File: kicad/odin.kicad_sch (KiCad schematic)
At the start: 0 parts

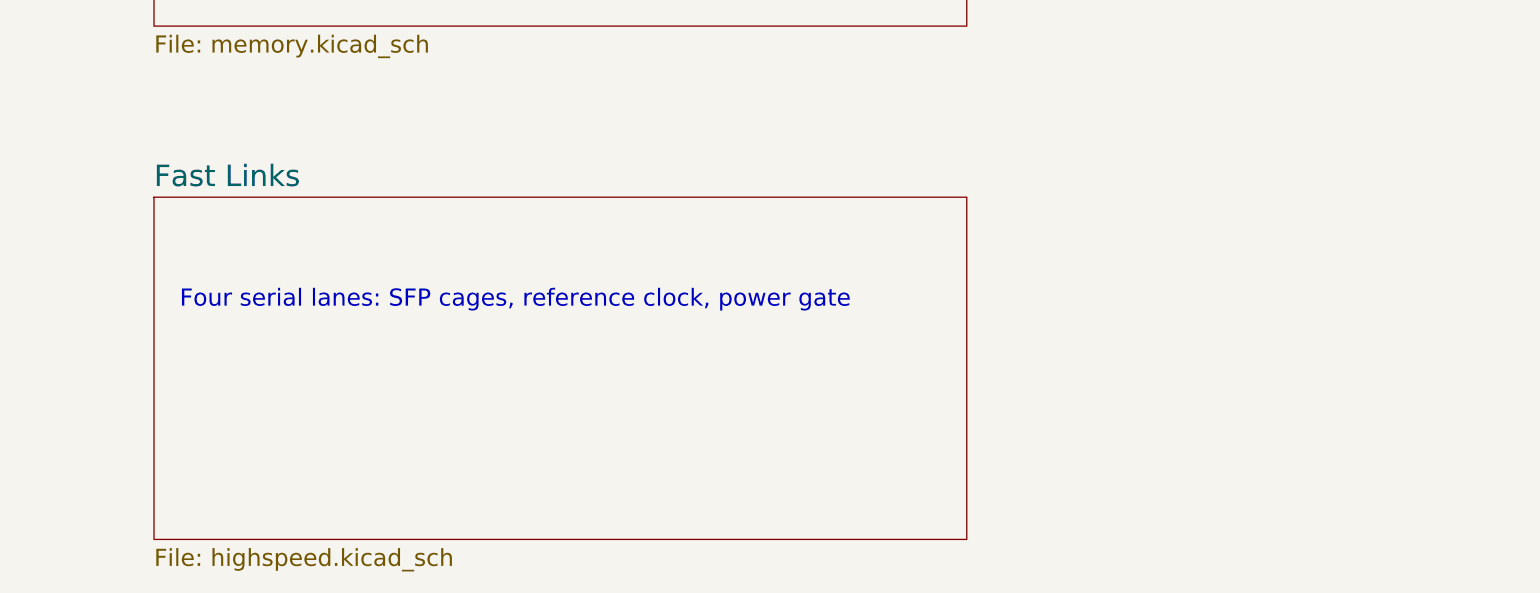
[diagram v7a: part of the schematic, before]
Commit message: Fast Links out, Network in: RTL8211FD-CG on RGMII, ETH jack, LINK P and LINK Q
The two SFP ports, their cages, the 125 MHz oscillator, the power gate and
the I2C switch leave the design, and with them the SFP nets on the board
controller (GPIO32-39 and 46 are spare, GPIO14/31 carry the status expander's
I2C). Both GTP quads stay powered per UG482 with grounded RX and one RCAL
each.

A Network sheet replaces them: an RTL8211FD-CG gigabit PHY on RGMII at 2.5 V
with its straps, reset, interrupt, MDIO pull-up, crystal and jack LEDs wired
from the datasheet rev 1.7 tables, a HanRun HR911130A 1000Base-T magjack,
and two plain shielded 8P8C jacks that carry eight DC-coupled LVDS_25 pairs
from bank 16 with ESD arrays at the jacks. The five new parts came in through
easyeda2kicad; two footprints the importer had shared with other parts got
their own copies, and the jacks' mounting holes are NPTH.

Bank 16 moves to +2V5 and tools/alloc.py allocates it shallowest-first with
the PHY receive clock on an MRCC ball and the two link receive clocks on
clock-capable pairs; both 5 V buses and the PHY control pins live in bank 13;
banks 13, 14 and 16 are depth sorted. Escape depth >= 7 drops from 58 to 50
balls. Docs: ref/network.md and ref/link-ports.md are new; the SFP pages are
gone; status LEDs, user manual, keep-outs and import checklist follow.
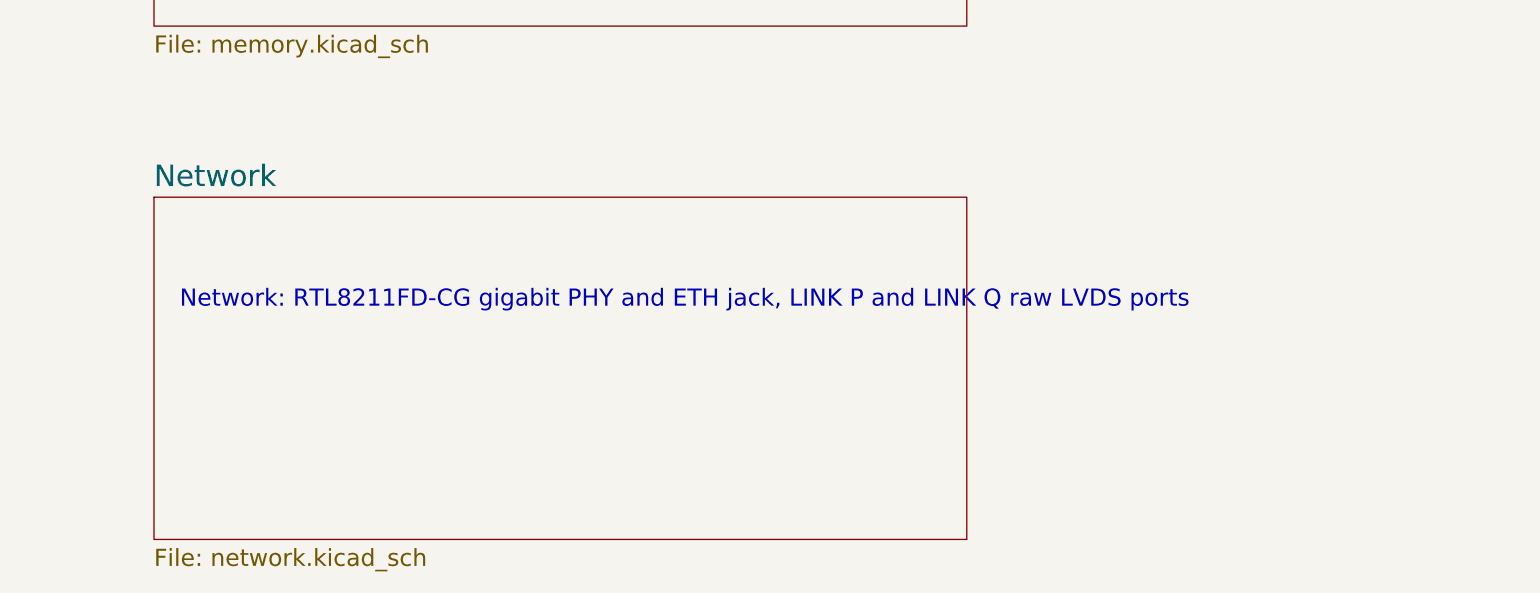
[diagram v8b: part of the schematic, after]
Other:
- removed sheet Fast Links
- added sheet Network (network.kicad_sch)
- note added: "Network: RTL8211FD-CG gigabit PHY and ETH jack, LINK P and LINK Q raw LVDS ports"
- note removed: "Four serial lanes: SFP cages, reference clock, power gate"
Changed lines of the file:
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@@
 	(sheet (at 270 115) (size 95 40)
 		(stroke (width 0.1524) (type solid)) (fill (color 0 0 0 0.0000))
-		(property "Sheetname" "Fast Links" (at 270 114 0) (effects (font (size 2.5 2.5)) (justify left bottom)))
-		(property "Sheetfile" "highspeed.kicad_sch" (at 270 156 0) (effects (font (size 2 2)) (justify left top)))
+		(property "Sheetname" "Network" (at 270 114 0) (effects (font (size 2.5 2.5)) (justify left bottom)))
+		(property "Sheetfile" "network.kicad_sch" (at 270 156 0) (effects (font (size 2 2)) (justify left top)))
 		(instances (project "odin" (path "/c44fb7fe-6133-ad34-68fd-fb66126197ef" (page "7"))))
 	)
-	(text "Four serial lanes: SFP cages, reference clock, power gate" (at 273 127 0) (effects (font (size 2 2)) (justify left)))
+	(text "Network: RTL8211FD-CG gigabit PHY and ETH jack, LINK P and LINK Q raw LVDS ports" (at 273 127 0) (effects (font (size 2 2)) (justify left)))
 	(sheet_instances (path "/" (page "1")))
 )
